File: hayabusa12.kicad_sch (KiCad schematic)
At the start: 32 parts, among them J1 USB_C_Receptacle_USB2.0, SW1 SW_Push, SW10 MX_SW_HS, SW11 MX_SW_HS, SW12 MX_SW_HS, SW13 MX_SW_HS, SW2 MX_SW_HS, SW3 MX_SW_HS, SW4 MX_SW_HS, SW5 MX_SW_HS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

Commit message: started routing
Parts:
- OL1: footprint kbd:OLED -> kbd:OLED_v2
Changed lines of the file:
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@@
       (effects (font (size 1.1938 1.1938)) (justify left))
     )
-    (property "Footprint" "kbd:OLED" (id 2) (at 245.11 59.69 0)
+    (property "Footprint" "kbd:OLED_v2" (id 2) (at 245.11 59.69 0)
       (effects (font (size 1.524 1.524)) hide)
     )
@@
     )
     (path "/b9768c68-15af-41b6-8061-376d6c0c72bb"
-      (reference "OL1") (unit 1) (value "OLED") (footprint "kbd:OLED")
+      (reference "OL1") (unit 1) (value "OLED") (footprint "kbd:OLED_v2")
     )
     (path "/c90e1c66-f02f-4505-9b26-a7ecf05f1ce3"

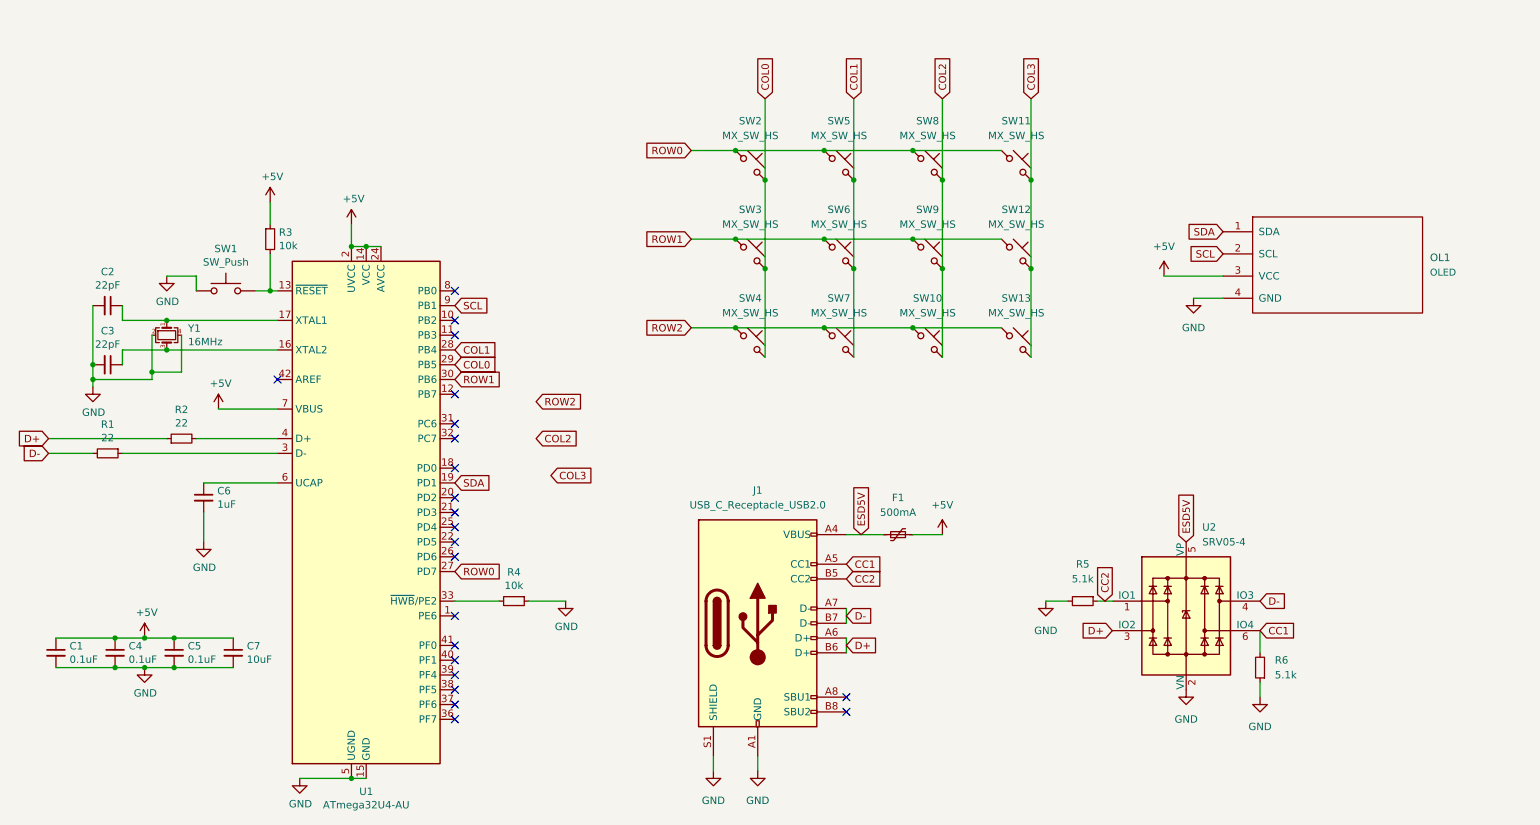
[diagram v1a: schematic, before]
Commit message: updated schematics
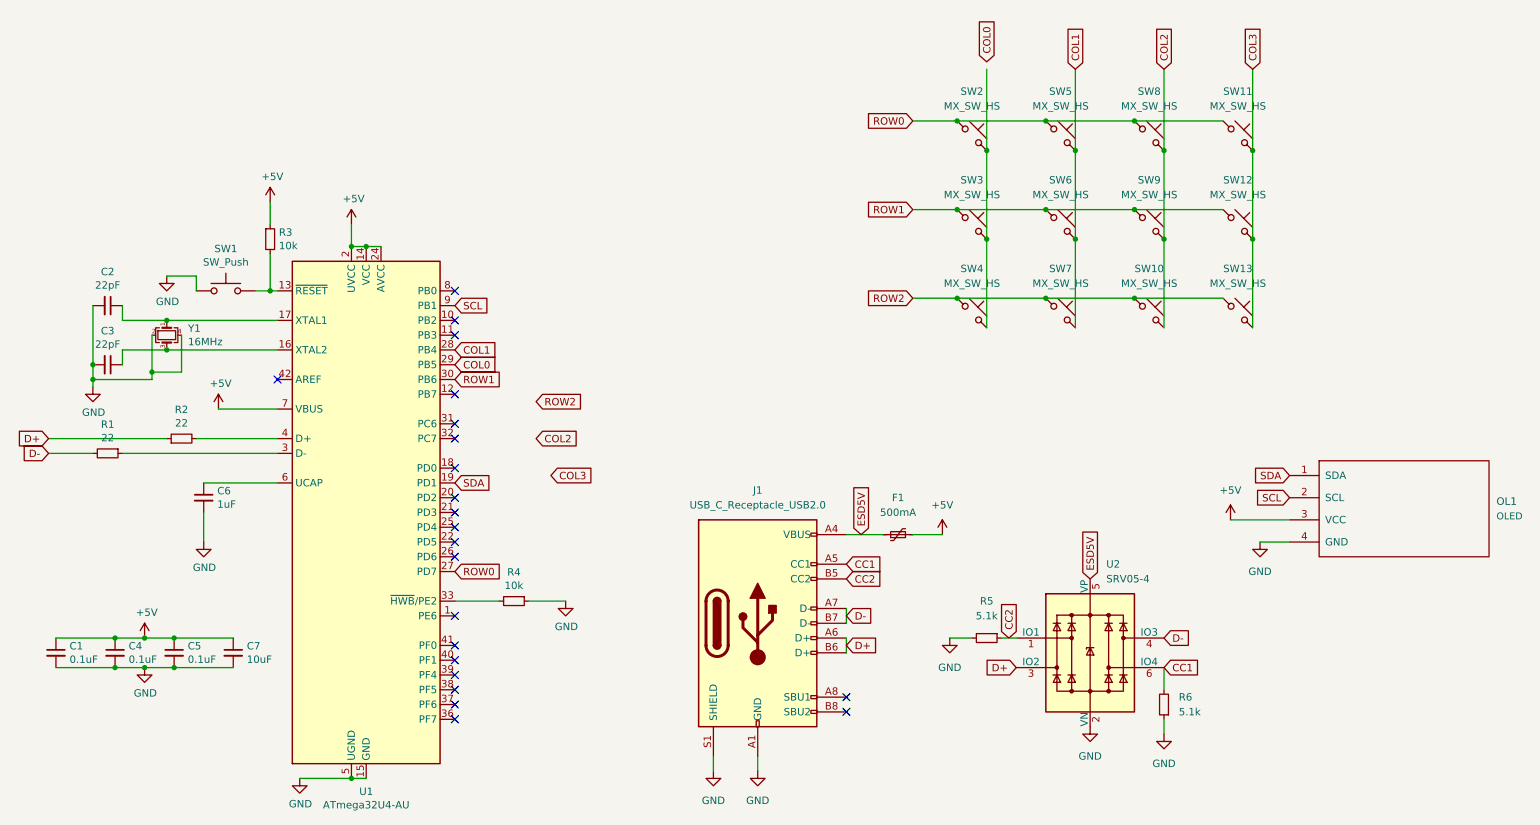
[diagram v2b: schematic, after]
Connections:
- net COL0: no longer SW2.2, SW3.2, SW4.2
- new net: SW2.2, SW3.2, SW4.2
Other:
- moved on the sheet: OL1, R5, R6, SW10, SW11, SW12, SW13, SW2, SW3, SW4, SW5, SW6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

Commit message: routing
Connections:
- net COL0: now also SW2.2, SW3.2, SW4.2, U1.31 (PC6); no longer U1.29 (PB5)
- net COL1: now also U1.30 (PB6); no longer U1.28 (PB4)
- net COL2: now also U1.29 (PB5)
- net COL3: now also U1.28 (PB4)
- net ROW0: now also U1.26 (PD6); no longer U1.27 (PD7)
- net ROW1: now also U1.27 (PD7); no longer U1.30 (PB6)
- net ROW2: now also U1.32 (PC7)
- no-connect marks 22 -> 19
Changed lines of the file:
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@@
   (no_connect (at 93.98 101.6))
   (no_connect (at 93.98 134.62))
-  (no_connect (at 93.98 91.44))
-  (no_connect (at 93.98 111.76))
   (no_connect (at 93.98 104.14))
   (no_connect (at 161.29 135.89))
@@
   (no_connect (at 63.5 81.28))
   (no_connect (at 93.98 132.08))
-  (no_connect (at 93.98 88.9))
   (wire (pts (xy 232.41 109.22) (xy 237.49 109.22))
     (stroke (width 0) (type default) (color 0 0 0 0))
@@
     (stroke (width 0) (type default) (color 0 0 0 0))
   )
+  (wire (pts (xy 210.82 36.83) (xy 226.06 36.83))
+    (stroke (width 0) (type default) (color 0 0 0 0))
+  )
   (wire (pts (xy 36.83 68.58) (xy 36.83 71.12))
     (stroke (width 0) (type default) (color 0 0 0 0))
@@
   )
   (wire (pts (xy 31.75 68.58) (xy 31.75 78.74))
-    (stroke (width 0) (type default) (color 0 0 0 0))
-  )
-  (wire (pts (xy 210.82 36.83) (xy 226.06 36.83))
     (stroke (width 0) (type default) (color 0 0 0 0))
   )
@@
     )
   )
-  (global_label "ROW0" (shape input) (at 93.98 114.3 0) (fields_autoplaced)
-    (effects (font (size 1.27 1.27)) (justify left))
-    (property "Intersheet References" "${INTERSHEET_REFS}" (id 0) (at 1.27 7.62 0)
+  (global_label "ROW0" (shape input) (at 93.98 111.76 0) (fields_autoplaced)
+    (effects (font (size 1.27 1.27)) (justify left))
+    (property "Intersheet References" "${INTERSHEET_REFS}" (id 0) (at 1.27 5.08 0)
       (effects (font (size 1.27 1.27)) hide)
     )
@@
     )
   )
-  (global_label "COL1" (shape input) (at 93.98 76.2 0) (fields_autoplaced)
-    (effects (font (size 1.27 1.27)) (justify left))
-    (property "Intersheet References" "${INTERSHEET_REFS}" (id 0) (at 1.27 7.62 0)
+  (global_label "COL1" (shape input) (at 93.98 81.28 0) (fields_autoplaced)
+    (effects (font (size 1.27 1.27)) (justify left))
+    (property "Intersheet References" "${INTERSHEET_REFS}" (id 0) (at 1.27 12.7 0)
       (effects (font (size 1.27 1.27)) hide)
     )
@@
     )
   )
-  (global_label "COL2" (shape input) (at 107.95 91.44 0) (fields_autoplaced)
-    (effects (font (size 1.27 1.27)) (justify left))
-    (property "Intersheet References" "${INTERSHEET_REFS}" (id 0) (at 115.2012 91.3606 0)
+  (global_label "COL2" (shape input) (at 93.98 78.74 0) (fields_autoplaced)
+    (effects (font (size 1.27 1.27)) (justify left))
+    (property "Intersheet References" "${INTERSHEET_REFS}" (id 0) (at 101.2312 78.6606 0)
       (effects (font (size 1.27 1.27)) (justify left) hide)
     )
@@
     )
   )
-  (global_label "ROW1" (shape input) (at 93.98 81.28 0) (fields_autoplaced)
-    (effects (font (size 1.27 1.27)) (justify left))
-    (property "Intersheet References" "${INTERSHEET_REFS}" (id 0) (at 1.27 7.62 0)
-      (effects (font (size 1.27 1.27)) hide)
-    )
-  )
-  (global_label "COL0" (shape input) (at 93.98 78.74 0) (fields_autoplaced)
-    (effects (font (size 1.27 1.27)) (justify left))
-    (property "Intersheet References" "${INTERSHEET_REFS}" (id 0) (at 1.27 7.62 0)
+  (global_label "ROW1" (shape input) (at 93.98 114.3 0) (fields_autoplaced)
+    (effects (font (size 1.27 1.27)) (justify left))
+    (property "Intersheet References" "${INTERSHEET_REFS}" (id 0) (at 1.27 40.64 0)
+      (effects (font (size 1.27 1.27)) hide)
+    )
+  )
+  (global_label "COL0" (shape input) (at 93.98 88.9 0) (fields_autoplaced)
+    (effects (font (size 1.27 1.27)) (justify left))
+    (property "Intersheet References" "${INTERSHEET_REFS}" (id 0) (at 1.27 17.78 0)
       (effects (font (size 1.27 1.27)) hide)
     )
@@
     )
   )
-  (global_label "COL3" (shape input) (at 110.49 97.79 0) (fields_autoplaced)
-    (effects (font (size 1.27 1.27)) (justify left))
-    (property "Intersheet References" "${INTERSHEET_REFS}" (id 0) (at 117.7412 97.7106 0)
+  (global_label "COL3" (shape input) (at 93.98 76.2 0) (fields_autoplaced)
+    (effects (font (size 1.27 1.27)) (justify left))
+    (property "Intersheet References" "${INTERSHEET_REFS}" (id 0) (at 101.2312 76.1206 0)
       (effects (font (size 1.27 1.27)) (justify left) hide)
     )
@@
     )
   )
-  (global_label "COL0" (shape input) (at 185.42 26.67 90) (fields_autoplaced)
-    (effects (font (size 1.27 1.27)) (justify left))
-    (property "Intersheet References" "${INTERSHEET_REFS}" (id 0) (at 30.48 -39.37 0)
+  (global_label "COL0" (shape input) (at 185.42 27.94 90) (fields_autoplaced)
+    (effects (font (size 1.27 1.27)) (justify left))
+    (property "Intersheet References" "${INTERSHEET_REFS}" (id 0) (at 30.48 -38.1 0)
       (effects (font (size 1.27 1.27)) hide)
     )
@@
     )
   )
-  (global_label "ROW2" (shape input) (at 107.95 85.09 0) (fields_autoplaced)
-    (effects (font (size 1.27 1.27)) (justify left))
-    (property "Intersheet References" "${INTERSHEET_REFS}" (id 0) (at 115.6245 85.0106 0)
-      (effects (font (size 1.27 1.27)) (justify left) hide)
-    )
+  (global_label "ROW2" (shape input) (at 93.98 91.44 0) (fields_autoplaced)
+    (effects (font (size 1.27 1.27)) (justify left))
+    (property "Intersheet References" "${INTERSHEET_REFS}" (id 0) (at 101.6545 91.3606 0)
+      (effects (font (size 1.27 1.27)) (justify left) hide)
+    )

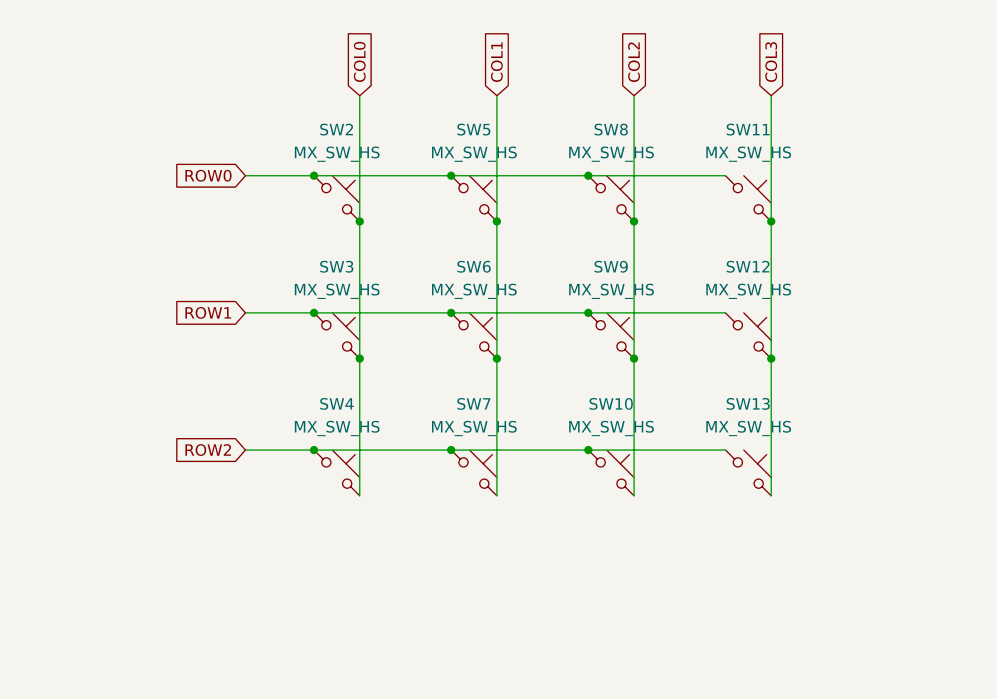
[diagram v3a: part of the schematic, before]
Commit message: added diodes bc i forgor
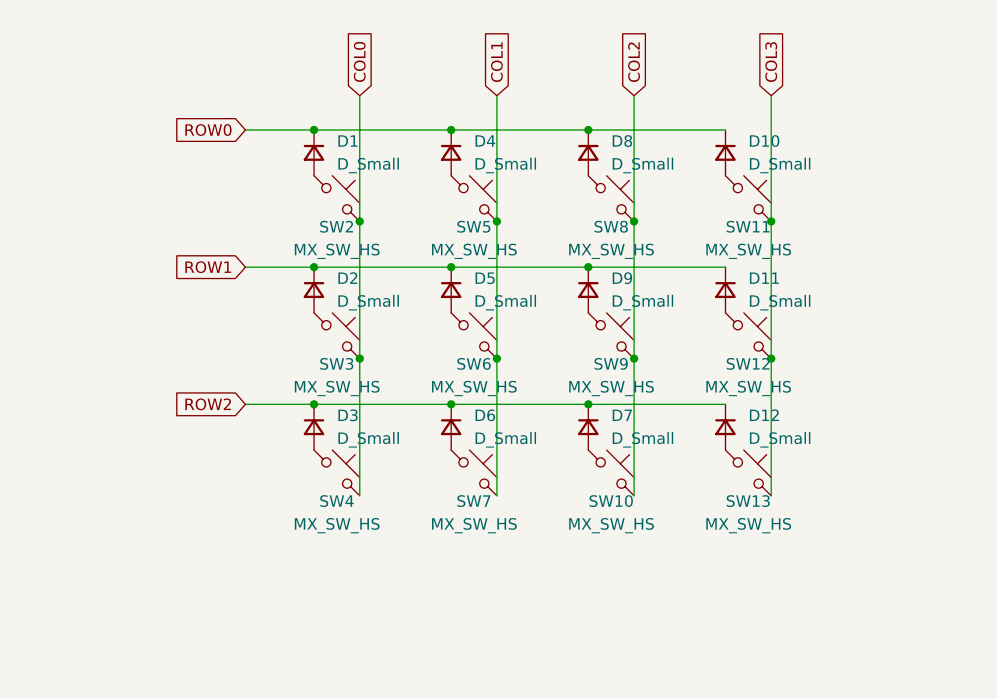
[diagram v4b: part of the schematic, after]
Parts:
- added D1, D10, D11, D12, D2, D3, D4, D5, D6, D7, D8, D9: D_Small, Diode_SMD:D_SOD-123, symbol Device:D_Small
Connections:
- net ROW0: now also D1.1 (K), D10.1 (K), D4.1 (K), D8.1 (K); no longer SW11.1, SW2.1, SW5.1, SW8.1
- net ROW1: now also D11.1 (K), D2.1 (K), D5.1 (K), D9.1 (K); no longer SW12.1, SW3.1, SW6.1, SW9.1
- net ROW2: now also D12.1 (K), D3.1 (K), D6.1 (K), D7.1 (K); no longer SW10.1, SW13.1, SW4.1, SW7.1
- new net: D11.2 (A), SW12.1
- new net: D12.2 (A), SW13.1
- new net: D6.2 (A), SW7.1
- new net: D10.2 (A), SW11.1
- new net: D9.2 (A), SW9.1
- new net: D1.2 (A), SW2.1
- new net: D5.2 (A), SW6.1
- new net: D4.2 (A), SW5.1
- new net: D8.2 (A), SW8.1
- new net: D2.2 (A), SW3.1
- new net: D7.2 (A), SW10.1
- new net: D3.2 (A), SW4.1

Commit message: cleaned up submodules
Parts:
- SW1: footprint random-keyboard-parts:SKQG-1155865 -> marbastlib-various:SW_SPST_SKQG_WithStem
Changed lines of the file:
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@@
     (property "Reference" "SW1" (id 0) (at 54.61 58.801 0))
     (property "Value" "SW_Push" (id 1) (at 54.61 61.1124 0))
-    (property "Footprint" "random-keyboard-parts:SKQG-1155865" (id 2) (at 54.61 60.96 0)
+    (property "Footprint" "marbastlib-various:SW_SPST_SKQG_WithStem" (id 2) (at 54.61 60.96 0)
       (effects (font (size 1.27 1.27)) hide)
     )
@@
     )
     (path "/0694356f-31fe-47cd-a767-adb061c8e560"
-      (reference "SW1") (unit 1) (value "SW_Push") (footprint "random-keyboard-parts:SKQG-1155865")
+      (reference "SW1") (unit 1) (value "SW_Push") (footprint "marbastlib-various:SW_SPST_SKQG_WithStem")
     )
     (path "/9a2c11a4-6958-4c2e-b9fc-b380a6e2ec2c"
